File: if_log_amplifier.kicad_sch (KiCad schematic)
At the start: 56 parts, among them J6 Conn_Coaxial, U301 AD603AQ, U302 L78L05_TO92, U303 LM317L_TO92, U304 AD8307AN, U305 CA3140

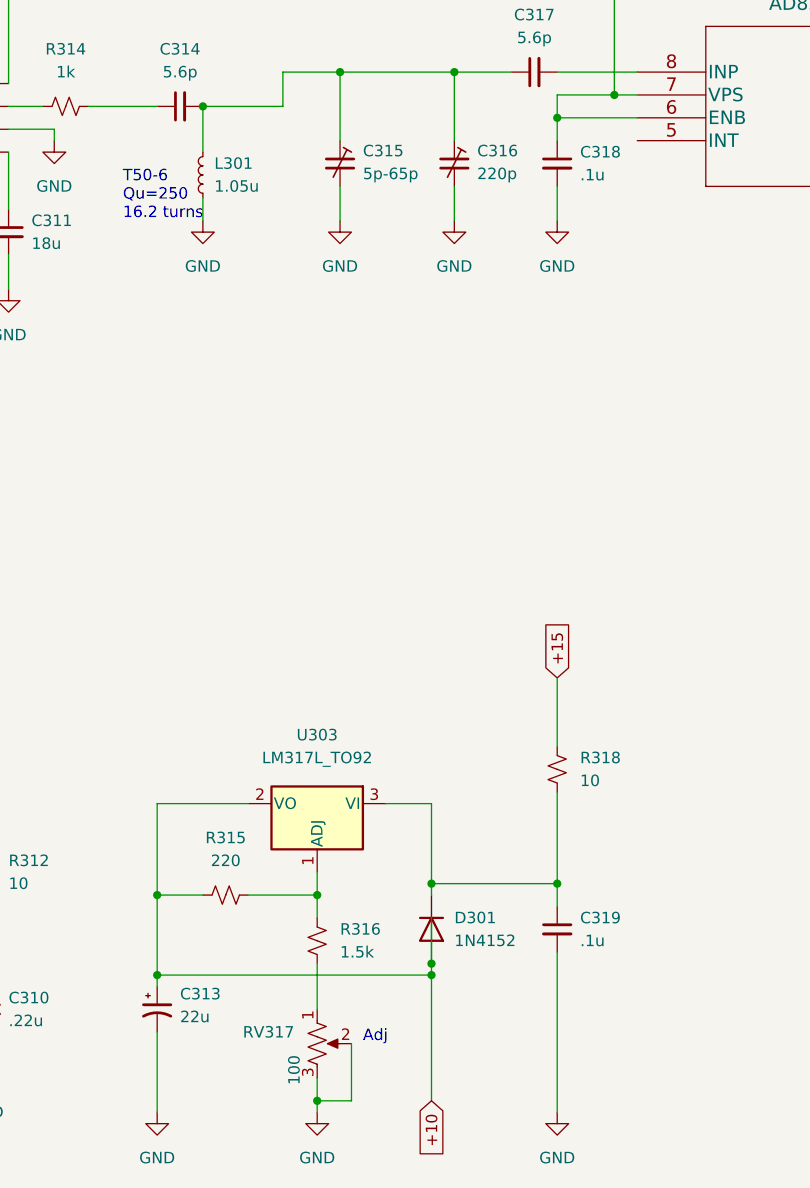
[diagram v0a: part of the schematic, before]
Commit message: updates to 15 v supply and if log amp boards
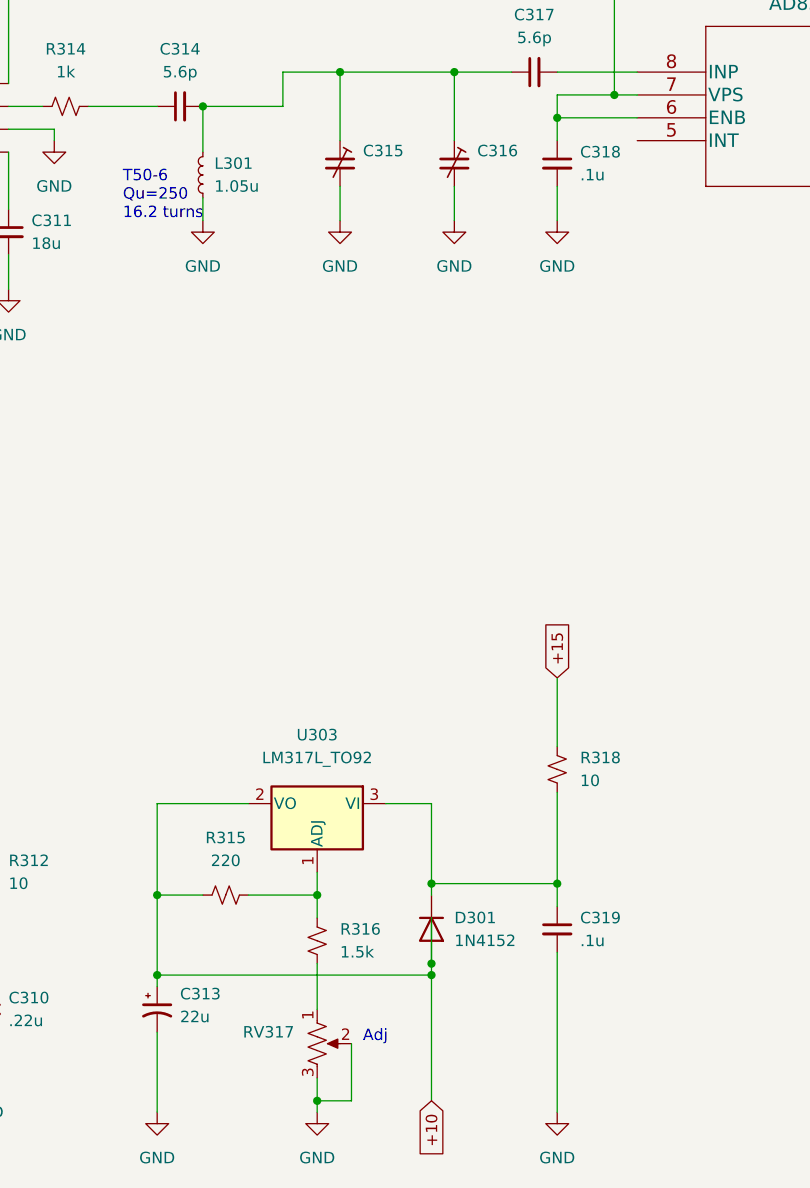
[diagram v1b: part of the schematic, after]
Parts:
- C315: value 5p-65p -> (none)
- C316: value 220p -> (none)
- RV317: value 100 -> (none)
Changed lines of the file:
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@@
       (effects (font (size 1.27 1.27)) (justify right))
     )
-    (property "Value" "100" (id 1) (at 162.56 177.7999 90)
+    (property "Value" "" (id 1) (at 162.56 177.7999 90)
       (effects (font (size 1.27 1.27)) (justify right))
     )
@@
       (effects (font (size 1.27 1.27)) (justify left))
     )
-    (property "Value" "5p-65p" (id 1) (at 170.18 79.8829 0)
+    (property "Value" "" (id 1) (at 170.18 79.8829 0)
       (effects (font (size 1.27 1.27)) (justify left))
     )
@@
       (effects (font (size 1.27 1.27)) (justify left))
     )
-    (property "Value" "220p" (id 1) (at 182.88 79.8829 0)
-      (effects (font (size 1.27 1.27)) (justify left))
-    )
+    (property "Value" "" (id 1) (at 182.88 79.8829 0)
+      (effects (font (size 1.27 1.27)) (justify left))
+    )

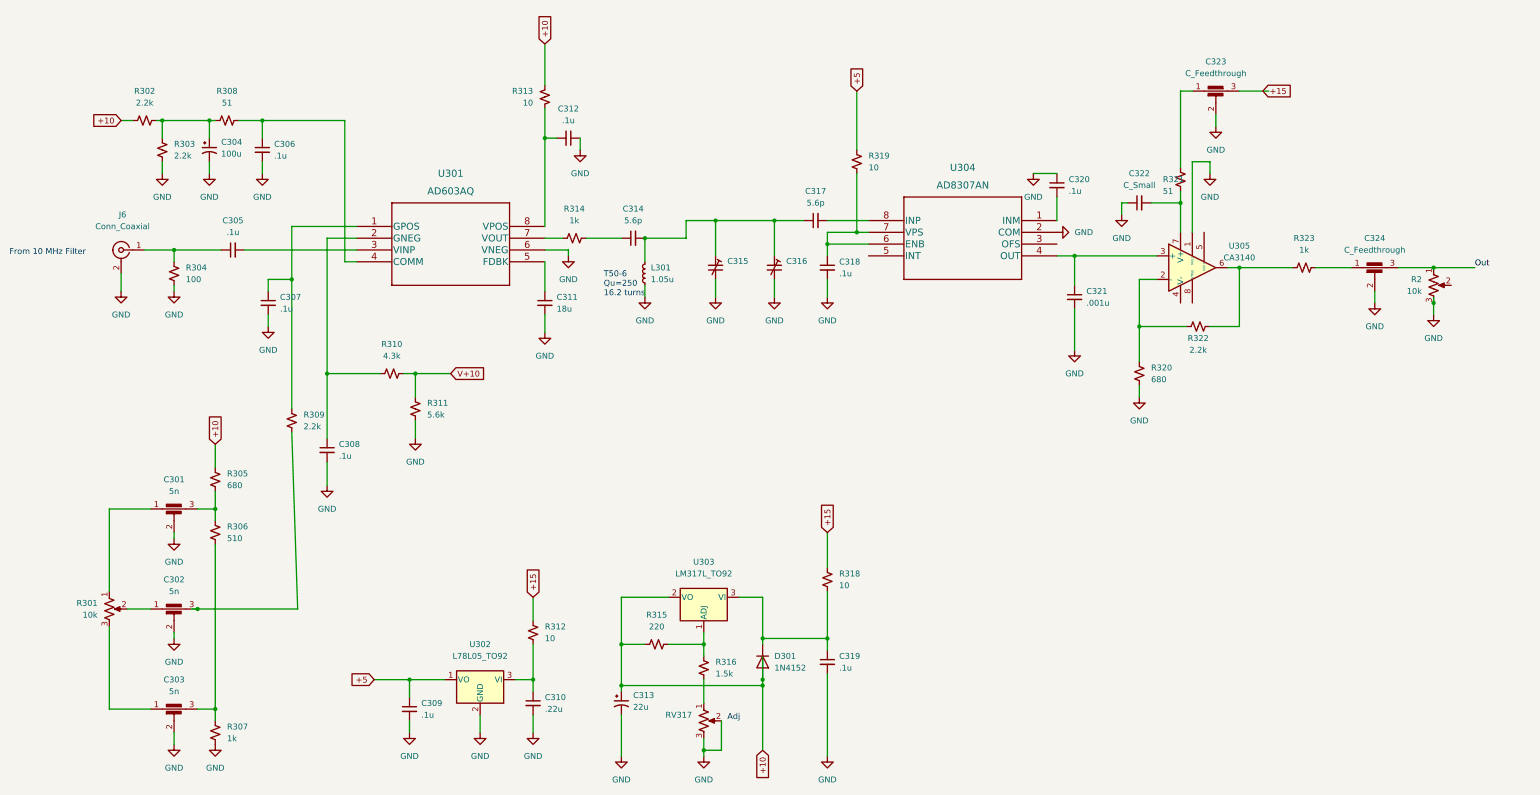
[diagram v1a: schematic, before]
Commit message: Significant changes to timebase spice, 15v supply and resolution-filters
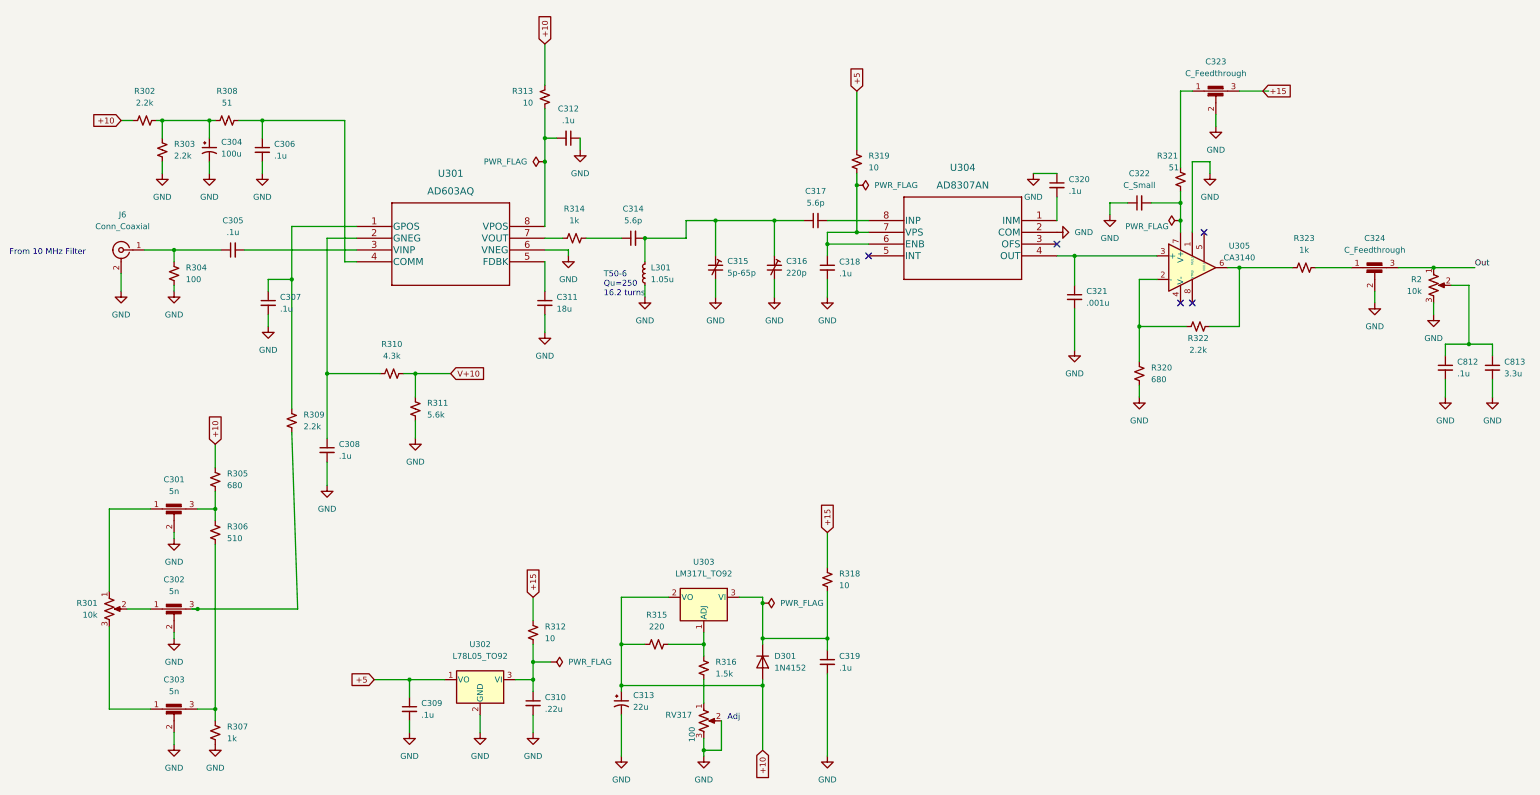
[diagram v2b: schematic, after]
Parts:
- added C812: .1u, symbol Device:C_Small
- added C813: 3.3u, symbol Device:C_Small
- C315: value (none) -> 5p-65p
- C316: value (none) -> 220p
- RV317: value (none) -> 100
- U301: symbol 2022-05-30_02-24-37:AD603AQ -> AD630AQ:AD603AQ
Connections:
- net GND: now also C812.2, C813.2
- net at R2.2: now also C812.1, C813.1
- no-connect marks 0 -> 5
